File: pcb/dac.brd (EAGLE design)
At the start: 100 x 80 mm, 10 parts, among them U1 PIC16F1773-I/SP

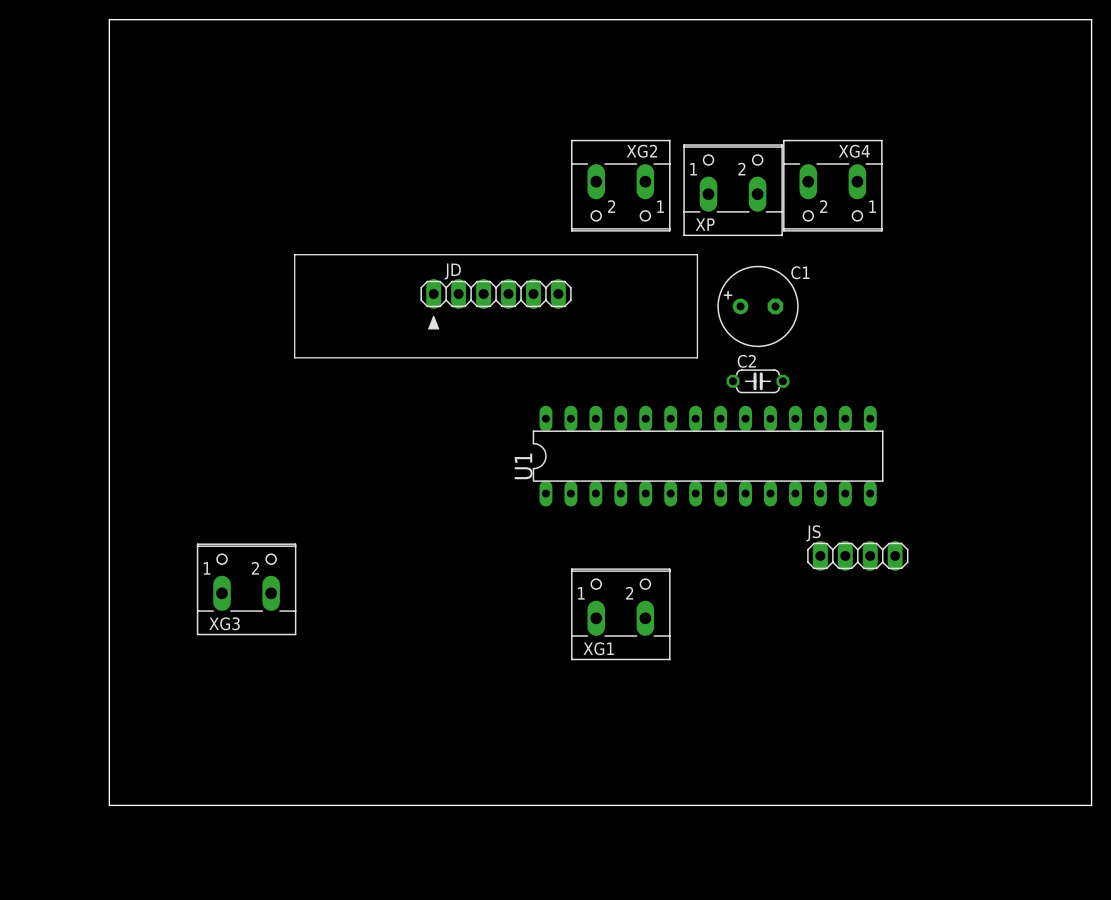
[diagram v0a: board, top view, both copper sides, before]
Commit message: Add fade circuit and a little firmware
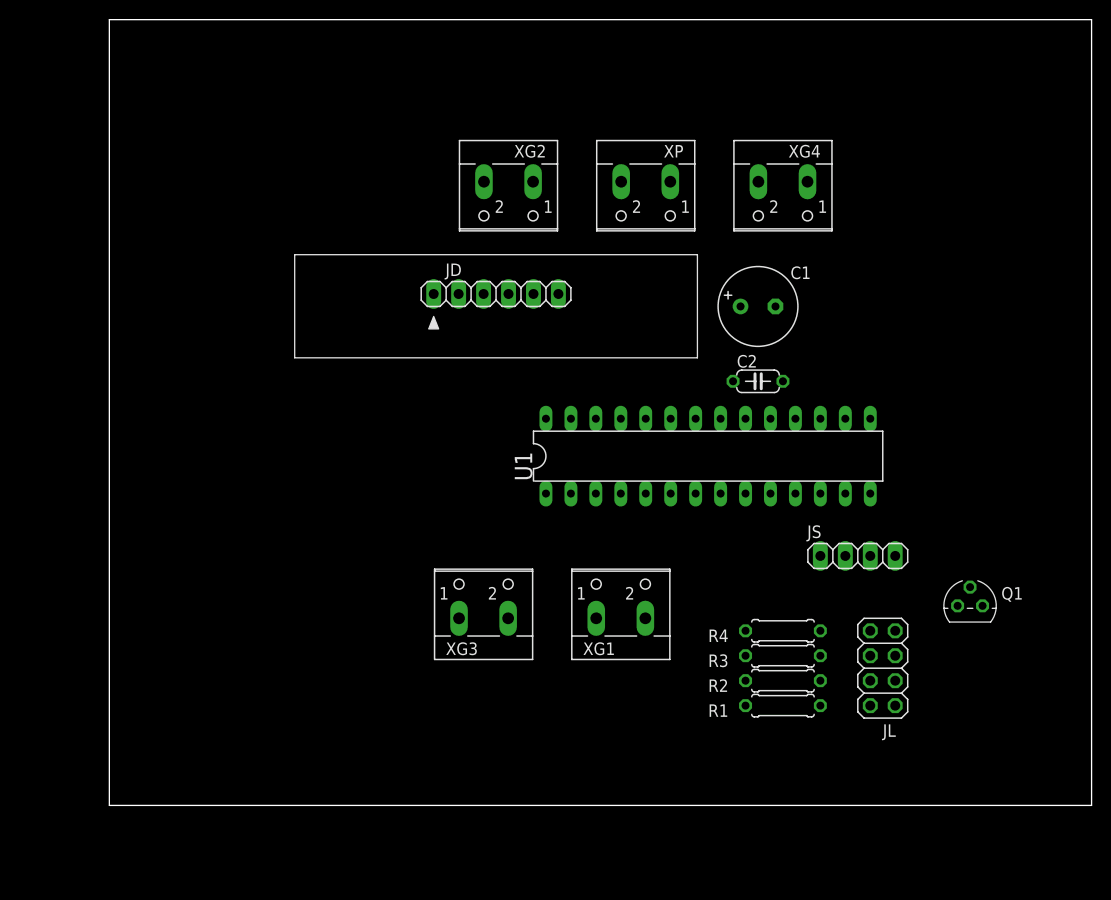
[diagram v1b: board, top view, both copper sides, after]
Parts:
- added JL: (no value), pinhead:2X04
- added Q1: 2N7000, transistor-fet:TO-92
- added R1, R2, R3, R4: 270R, rcl:0207/7
- moved XG3 24.3 mm to (38.1, 20.3)
- moved XG2 11.4 mm to (40.6, 62.2)
- moved XP 8.98 mm to (54.6, 62.2), turned to 180 degrees
- moved XG4 5.08 mm to (68.6, 62.2)
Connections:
- new net FADE: Q1.2, U1.15
- new net LED1: JL.2, R1.1
- new net LED2: JL.4, R2.1
- new net LED3: JL.6, R3.1
- new net LED4: JL.8, R4.1
- new net N$1: JL.1, JL.3, JL.5, JL.7, Q1.3
- net +5V: now also R1.2, R2.2, R3.2, R4.2
- net GND: now also Q1.1

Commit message: Increase LED drive current to 13mA
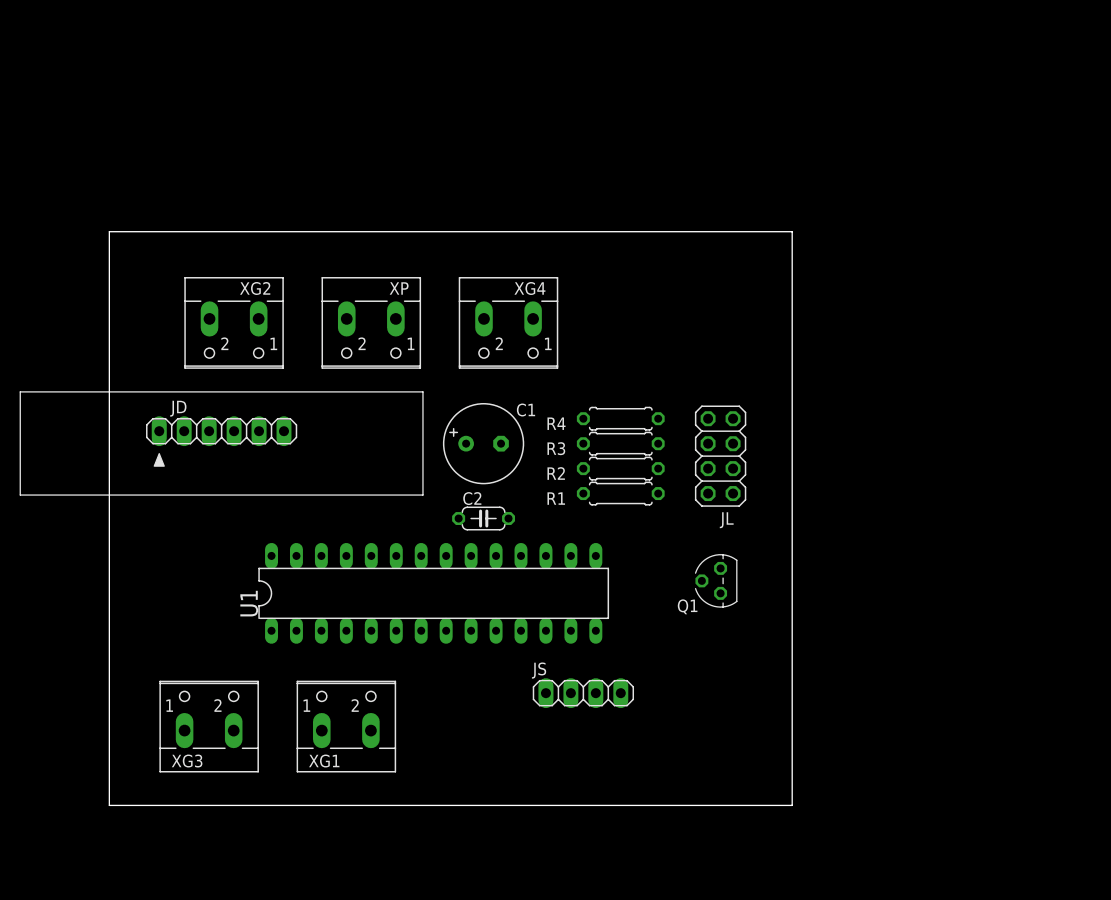
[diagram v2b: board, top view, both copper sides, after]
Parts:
- R1, R2, R3, R4: value 270R -> 220R
- moved C1 31.2 mm to (38.1, 36.8)
- moved C2 31.2 mm to (38.1, 29.2)
- moved JS 31.2 mm to (48.3, 11.4)
- moved XG2 31.2 mm to (12.7, 48.3)
- moved JD 31.2 mm to (11.4, 38.1)
- moved U1 31.2 mm to (33.0, 21.6)
- moved XG4 31.2 mm to (40.6, 48.3)
- moved XP 31.2 mm to (26.7, 48.3)
- moved XG1 30.2 mm to (24.1, 8.89)
- moved XG3 30.2 mm to (10.2, 8.89)
- moved JL 27.2 mm to (62.2, 35.6)
- moved R1 27.2 mm to (52.1, 31.8)
- moved R2 27.2 mm to (52.1, 34.3)
- moved R3 27.2 mm to (52.1, 36.8)
- moved R4 27.2 mm to (52.1, 39.4)
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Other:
- board size 100 x 80 mm -> 69.5 x 58.4 mm

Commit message: Protoboard layout & routing
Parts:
- removed JL: (no value), pinhead:2X04
- removed XG1, XG2, XG3, XG4: (no value), con-wago-500:W237-102
- added C3: 2.2uF, rcl:C050-024X044
- added D1: SA5.0A, diode:P1Z12
- added JG1H, JG1L, JG2H, JG2L, JG4H, JG4L, JG5H, JG5L: (no value), pinhead:1X01
- added JPH: (no value), pinhead:1X04
- added JPL: (no value), pinhead:1X03
- added U2: MCP6002-I/P, linear:DIL08
- R1, R2, R3, R4: device rcl:0207/7 -> rcl:0207/2V
- moved JD 47.0 mm to (58.4, 36.8), turned to 270 degrees
- moved R4 30.9 mm to (62.2, 10.2)
- moved R3 26.2 mm to (62.2, 12.7)
- moved C1 23.9 mm to (15.2, 43.8), turned to 270 degrees
- moved XP 23.4 mm to (3.81, 43.2), turned to 270 degrees
- moved Q1 22.6 mm to (48.3, 5.08)
- moved R2 21.6 mm to (62.2, 15.2)
- moved JS 18.5 mm to (30.5, 6.35), turned to 270 degrees
- moved R1 17.3 mm to (62.2, 17.8)
- moved C2 17.1 mm to (50.8, 17.8)
- moved U1 6.35 mm to (39.4, 21.6), turned to 270 degrees
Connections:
- removed net N$1: JL.1, JL.3, JL.5, JL.7, Q1.3
- new net DAC1_UNBUF: U1.3, U2.5
- new net FADE_L: JPL.1, JPL.2, JPL.3, Q1.3
- net +5V: now also C3.1, D1.C, R1.1, R2.1, R3.1, R4.1, U2.8; no longer R1.2, R2.2, R3.2, R4.2
- net DAC1: now also JG1H.1, U2.6, U2.7; no longer U1.3, XG1.1
- net DAC2: now also JG2H.1; no longer XG2.1
- net DAC4: now also JG4H.1, U2.1, U2.2; no longer XG3.1
- net DAC4_UNBUF: now also U2.3
- net DAC5: now also JG5H.1; no longer XG4.1
- net GND: now also C3.2, D1.A, JG1L.1, JG2L.1, JG4L.1, JG5L.1, U2.4; no longer XG1.2, XG2.2, XG3.2, XG4.2
- net LED1: now also JPH.1, R1.2; no longer JL.2, R1.1
- net LED2: now also JPH.2, R2.2; no longer JL.4, R2.1
- net LED3: now also JPH.3, R3.2; no longer JL.6, R3.1
- net LED4: now also JPH.4, R4.2; no longer JL.8, R4.1
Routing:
- net GND: track 0.00 -> 284.5 mm
- net +5V: track 0.00 -> 279.4 mm
- net DAC1_UNBUF: track 0.00 -> 10.2 mm
- net DAC4_UNBUF: track 0.00 -> 10.2 mm
- net DAC1: track 0.00 -> 10.2 mm
- net !MCLR: track 0.00 -> 10.2 mm
- net PGD: track 0.00 -> 10.2 mm
- net PGC: track 0.00 -> 10.2 mm
- net DAC4: track 0.00 -> 10.2 mm
- net SCLK: track 0.00 -> 5.08 mm
- net MOSI: track 0.00 -> 5.08 mm
- net MISO: track 0.00 -> 5.08 mm
- net LED4: track 0.00 -> 5.08 mm
- net LED3: track 0.00 -> 5.08 mm
- net LED2: track 0.00 -> 5.08 mm
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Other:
- board size 69.5 x 58.4 mm -> 66 x 63.5 mm
- board text added: "www.PROTO-ADVANTAGE.com SBB1605-1"

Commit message: Notes on diffusion angle and lighting
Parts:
- added RP: 100R, rcl:0207/2V
- JPH: device pinhead:1X04 -> pinhead:1X05
- R1, R2, R4, R5: value 220R -> 100R
- moved R4 5.08 mm to (62.2, 15.2)
- moved R2 2.54 mm to (62.2, 17.8)
- moved R1 2.54 mm to (62.2, 20.3)
- moved JPH 1.27 mm to (58.4, 15.2)
- renumbered R3 to R5
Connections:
- new net N$1: JPH.5, RP.2
- net +5V: now also RP.1
- net LED3: now also R4.2; no longer R5.2
- net LED4: now also R5.2; no longer R4.2
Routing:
- net N$1: track 0.00 -> 5.08 mm

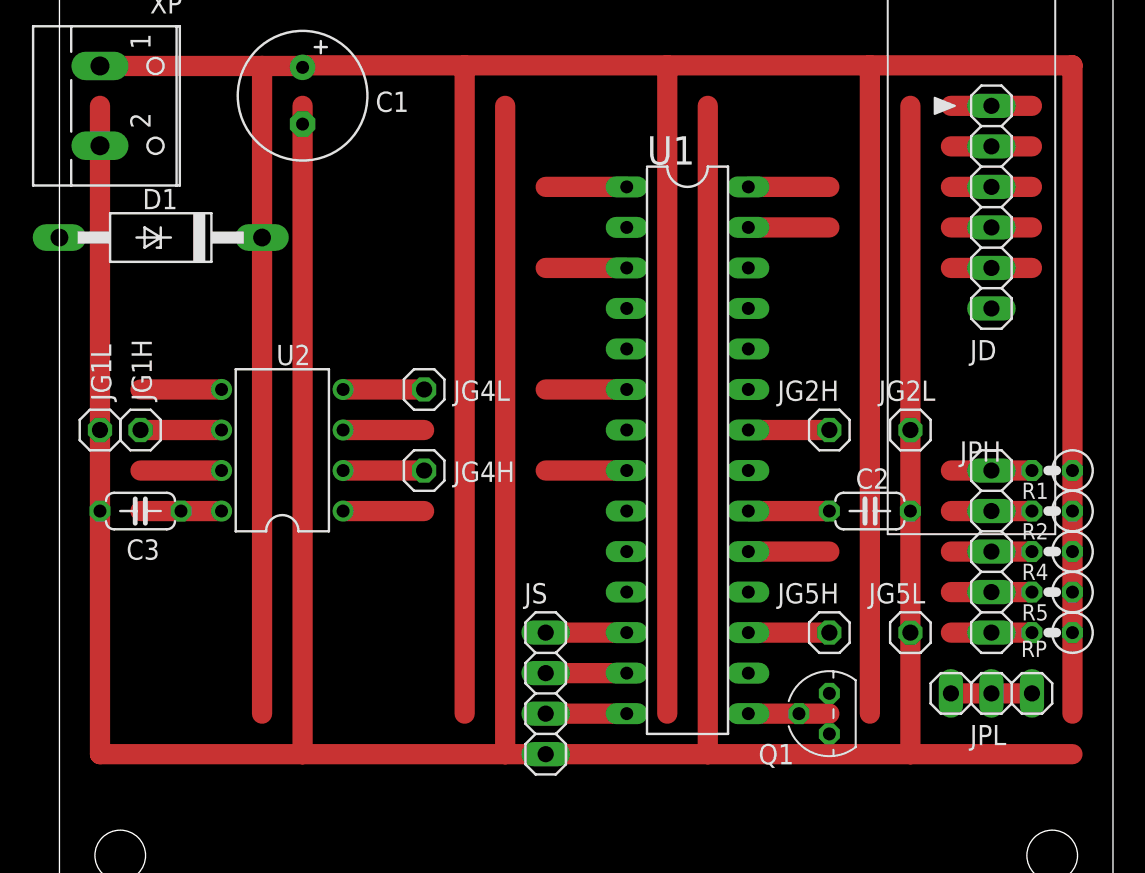
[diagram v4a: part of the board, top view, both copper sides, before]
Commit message: MISO pullup, minor cleanup
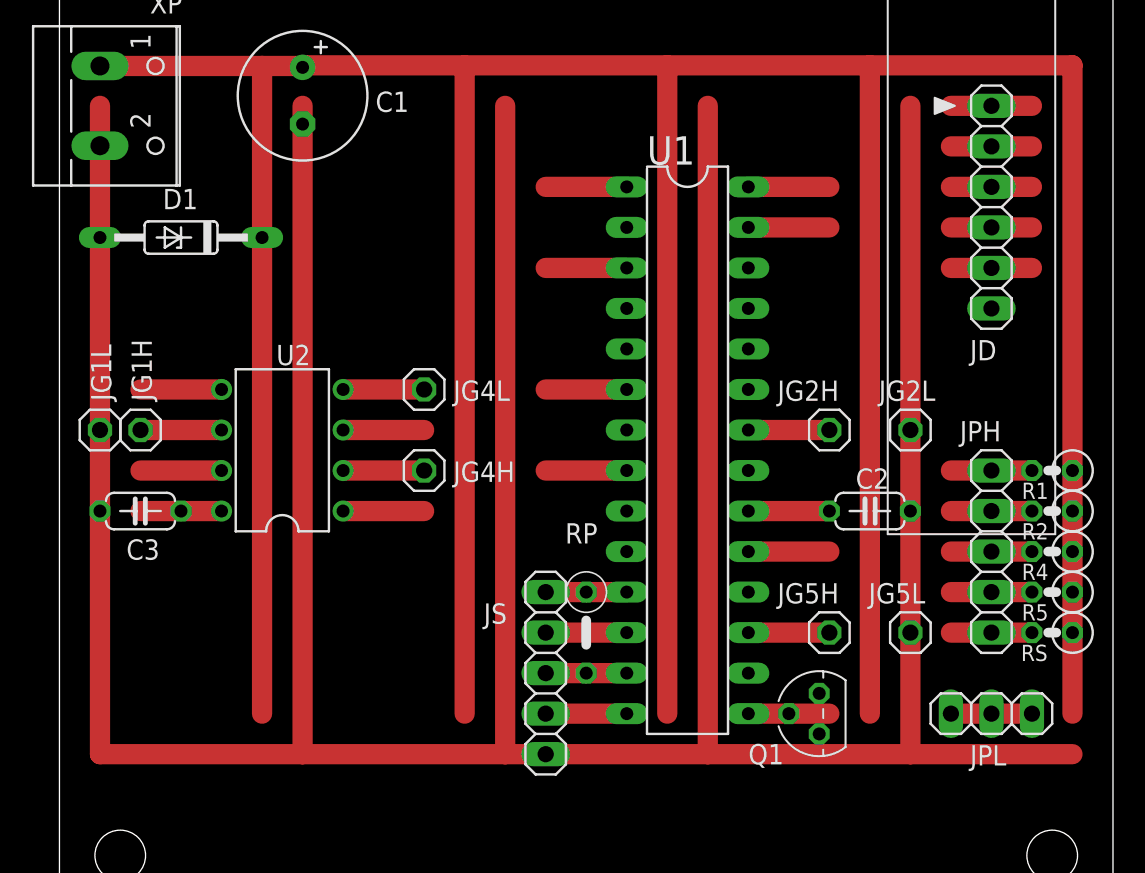
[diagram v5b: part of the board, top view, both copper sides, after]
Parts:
- added RS: 1k, rcl:0207/2V
- D1: device diode:P1Z12 -> diode:DO35Z10
- JS: device pinhead:1X04 -> pinhead:1X05
- RP: value 100R -> 1k; device rcl:0207/2V -> rcl:0207/5V
- moved RP 29.2 mm to (33.0, 10.2), turned to 270 degrees
- moved D1 1.27 mm to (7.62, 34.9)
- moved JS 1.27 mm to (30.5, 7.62)
- moved JPL 1.27 mm to (58.4, 5.08)
- moved Q1 0.63 mm to (47.6, 5.08)
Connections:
- removed net LED3: JPH.3, R4.2
- removed net N$1: JPH.5, RP.2
- new net +3V3: JS.1, RP.1, U1.11
- new net LED5: JPH.4, R5.2
- new net LEDSUP: JPH.5, RS.2
- net +5V: now also RS.1; no longer RP.1
- net GND: now also JS.5; no longer JS.4
- net LED4: now also JPH.3, R4.2; no longer JPH.4, R5.2
- net MISO: now also JS.3, RP.2; no longer JS.2
- net MOSI: now also JS.2; no longer JS.1
- net SCLK: now also JS.4; no longer JS.3
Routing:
- net +3V3: track 0.00 -> 5.08 mm
- net N$1: track 5.08 -> 0.00 mm
- net LEDSUP: track 0.00 -> 5.08 mm
- net LED5: track 0.00 -> 5.08 mm
- net LED3: track 5.08 -> 0.00 mm

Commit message: Drop FET driver for LEDs; switch to HIDRV on B0 in open-drain mode; LEDs in serial
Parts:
- removed Q1: 2N7000, transistor-fet:TO-92
- removed R1, R2: 100R, rcl:0207/2V
- JPH: device pinhead:1X05 -> pinhead:1X03
- JPL: device pinhead:1X03 -> pinhead:1X02
- R12, R45: value 100R -> 47R
- RS: value 1k -> 2.2k
- moved JPL 19.1 mm to (47.0, 20.3)
- moved JPH 2.54 mm to (58.4, 12.7)
- renumbered R4 to R12, R5 to R45
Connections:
- removed net FADE_L: JPL.1, JPL.2, JPL.3, Q1.3
- removed net LED4: JPH.3, R12.2
- removed net LED5: JPH.4, R45.2
- net +5V: no longer R1.1, R2.1
- net FADE: now also JPL.1, JPL.2, U1.21; no longer Q1.2, U1.15
- net GND: no longer Q1.1
- net LED1: now also R12.2; no longer R1.2
- net LED2: now also R45.2; no longer R2.2
- net LEDSUP: now also JPH.3; no longer JPH.5
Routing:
- net LED5: track 5.08 -> 0.00 mm
- net LED4: track 5.08 -> 0.00 mm
- net FADE_L: track 5.08 -> 0.00 mm

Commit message: Get closer to 30mA based on a parallel approximation; parts on hand and whatnot
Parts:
- R12, R45: value 47R -> 38R
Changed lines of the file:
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@@
 <attribute name="VALUE" x="27.305" y="12.7" size="1.27" layer="27" rot="R270"/>
 </element>
-<element name="R12" library="rcl" library_urn="urn:adsk.eagle:library:334" package="0207/2V" package3d_urn="urn:adsk.eagle:package:23490/1" value="47R" x="62.23" y="15.24" smashed="yes" rot="R180">
+<element name="R12" library="rcl" library_urn="urn:adsk.eagle:library:334" package="0207/2V" package3d_urn="urn:adsk.eagle:package:23490/1" value="38R" x="62.23" y="15.24" smashed="yes" rot="R180">
 <attribute name="NAME" x="60.325" y="13.462" size="1.016" layer="25" ratio="10"/>
 <attribute name="POPULARITY" value="0" x="62.23" y="15.24" size="1.778" layer="27" rot="R180" display="off"/>
@@
 <attribute name="VALUE" x="60.579" y="17.2212" size="1.27" layer="27" ratio="10"/>
 </element>
-<element name="R45" library="rcl" library_urn="urn:adsk.eagle:library:334" package="0207/2V" package3d_urn="urn:adsk.eagle:package:23490/1" value="47R" x="62.23" y="12.7" smashed="yes" rot="R180">
+<element name="R45" library="rcl" library_urn="urn:adsk.eagle:library:334" package="0207/2V" package3d_urn="urn:adsk.eagle:package:23490/1" value="38R" x="62.23" y="12.7" smashed="yes" rot="R180">
 <attribute name="NAME" x="60.325" y="10.922" size="1.016" layer="25" ratio="10"/>
 <attribute name="POPULARITY" value="0" x="62.23" y="12.7" size="1.778" layer="27" rot="R180" display="off"/>

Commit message: Ended up using 1k for power indicator; journal entry
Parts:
- RS: value 2.2k -> 1k
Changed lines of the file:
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@@
 <attribute name="VALUE" x="52.07" y="6.985" size="1.27" layer="27"/>
 </element>
-<element name="RS" library="rcl" library_urn="urn:adsk.eagle:library:334" package="0207/2V" package3d_urn="urn:adsk.eagle:package:23490/1" value="2.2k" x="62.23" y="10.16" smashed="yes" rot="R180">
+<element name="RS" library="rcl" library_urn="urn:adsk.eagle:library:334" package="0207/2V" package3d_urn="urn:adsk.eagle:package:23490/1" value="1k" x="62.23" y="10.16" smashed="yes" rot="R180">
 <attribute name="NAME" x="60.2742" y="8.382" size="1.016" layer="25" ratio="10"/>
 <attribute name="POPULARITY" value="0" x="62.23" y="10.16" size="1.778" layer="27" rot="R180" display="off"/>
